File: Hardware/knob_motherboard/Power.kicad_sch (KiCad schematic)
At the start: 16 parts, among them J1 USB_C_Receptacle_USB2.0, U4 CH224K, U6 MT2492

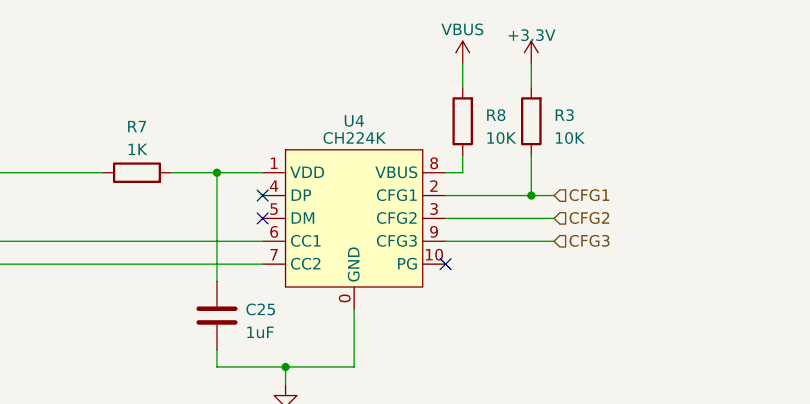
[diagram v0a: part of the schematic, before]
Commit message: drv8311 spi bugfix & ch224k CFG1 bugfix
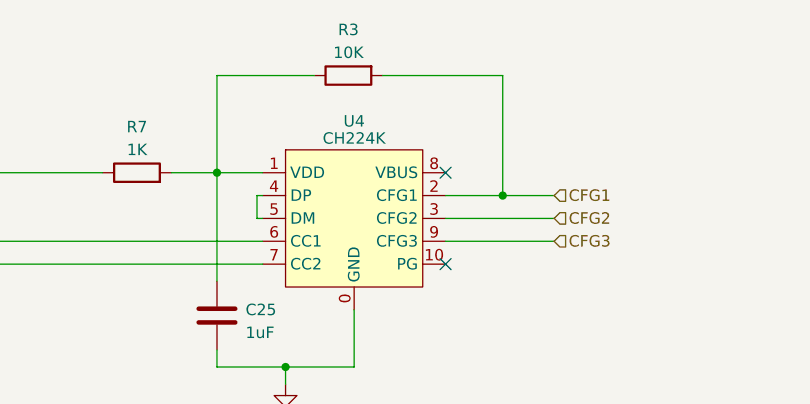
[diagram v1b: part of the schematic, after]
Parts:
- removed R8: 10K, Resistor_SMD:R_0402_1005Metric, symbol Device:R
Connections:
- net +3.3V is gone; now on net CFG1: R3.2
- net CFG1: no longer R3.1
- net at C25.1, R7.2, U4.1 (VDD): now also R3.1
- net at U4.4 (DP): now also U4.5 (DM)
- no-connect marks 5 -> 4
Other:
- moved on the sheet: R3
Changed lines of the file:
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@@
     (company "wirano")
   )
+  (junction (at 119.38 86.36) (diameter 0) (color 0 0 0 0)
+  )
   (junction (at 87.63 83.82) (diameter 0) (color 0 0 0 0)
-  )
-  (junction (at 122.555 86.36) (diameter 0) (color 0 0 0 0)
   )
   (junction (at 253.365 95.25) (diameter 0) (color 0 0 0 0)
@@
   (no_connect (at 57.15 116.84))
   (no_connect (at 113.03 93.98))
-  (no_connect (at 92.71 86.36))
-  (no_connect (at 92.71 88.9))
+  (no_connect (at 113.03 83.82))
   (wire (pts (xy 102.87 99.06) (xy 102.87 105.41))
     (stroke (width 0) (type default))
@@
     (stroke (width 0) (type default))
   )
-  (wire (pts (xy 114.935 81.915) (xy 114.935 83.82))
-    (stroke (width 0) (type default))
-  )
   (wire (pts (xy 34.29 124.46) (xy 34.29 125.73))
     (stroke (width 0) (type default))
@@
     (stroke (width 0) (type default))
   )
-  (wire (pts (xy 122.555 71.755) (xy 122.555 74.295))
-    (stroke (width 0) (type default))
-  )
   (wire (pts (xy 125.095 88.9) (xy 113.03 88.9))
     (stroke (width 0) (type default))
@@
     (stroke (width 0) (type default))
   )
-  (wire (pts (xy 113.03 83.82) (xy 114.935 83.82))
-    (stroke (width 0) (type default))
-  )
   (wire (pts (xy 266.7 95.25) (xy 266.7 92.71))
     (stroke (width 0) (type default))
@@
     (stroke (width 0) (type default))
   )
-  (wire (pts (xy 125.095 86.36) (xy 122.555 86.36))
-    (stroke (width 0) (type default))
-  )
   (wire (pts (xy 266.7 95.25) (xy 253.365 95.25))
     (stroke (width 0) (type default))
@@
     (stroke (width 0) (type default))
   )
-  (wire (pts (xy 114.935 71.755) (xy 114.935 74.295))
+  (wire (pts (xy 119.38 86.36) (xy 125.095 86.36))
     (stroke (width 0) (type default))
   )
@@
     (stroke (width 0) (type default))
   )
+  (wire (pts (xy 106.045 73.025) (xy 119.38 73.025))
+    (stroke (width 0) (type default))
+  )
   (wire (pts (xy 241.935 114.935) (xy 241.935 109.855))
     (stroke (width 0) (type default))
@@
     (stroke (width 0) (type default))
   )
+  (wire (pts (xy 92.075 86.36) (xy 92.075 88.9))
+    (stroke (width 0) (type default))
+  )
   (wire (pts (xy 222.885 95.25) (xy 233.045 95.25))
     (stroke (width 0) (type default))
@@
     (stroke (width 0) (type default))
   )
+  (wire (pts (xy 92.075 88.9) (xy 92.71 88.9))
+    (stroke (width 0) (type default))
+  )
+  (wire (pts (xy 119.38 73.025) (xy 119.38 86.36))
+    (stroke (width 0) (type default))
+  )
   (wire (pts (xy 253.365 102.235) (xy 253.365 95.25))
     (stroke (width 0) (type default))
@@
     (stroke (width 0) (type default))
   )
+  (wire (pts (xy 87.63 73.025) (xy 98.425 73.025))
+    (stroke (width 0) (type default))
+  )
   (wire (pts (xy 210.185 83.82) (xy 210.185 95.25))
     (stroke (width 0) (type default))
@@
     (stroke (width 0) (type default))
   )
-  (wire (pts (xy 113.03 86.36) (xy 122.555 86.36))
+  (wire (pts (xy 92.075 86.36) (xy 92.71 86.36))
+    (stroke (width 0) (type default))
+  )
+  (wire (pts (xy 113.03 86.36) (xy 119.38 86.36))
     (stroke (width 0) (type default))
   )
@@
     (stroke (width 0) (type default))
   )
+  (wire (pts (xy 87.63 73.025) (xy 87.63 83.82))
+    (stroke (width 0) (type default))
+  )
   (wire (pts (xy 95.25 105.41) (xy 95.25 107.315))
     (stroke (width 0) (type default))
@@
   )
   (wire (pts (xy 233.045 95.25) (xy 241.935 95.25))
-    (stroke (width 0) (type default))
-  )
-  (wire (pts (xy 122.555 81.915) (xy 122.555 86.36))
     (stroke (width 0) (type default))
   )
@@
     (effects (font (size 1.27 1.27)) (justify left))
   )
-  (symbol (lib_id "Device:R") (at 122.555 78.105 180) (unit 1)
-    (in_bom yes) (on_board yes) (dnp no) (fields_autoplaced)
-    (property "Reference" "R3" (at 125.095 77.47 0)
-      (effects (font (size 1.27 1.27)) (justify right))
-    )
-    (property "Value" "10K" (at 125.095 80.01 0)
-      (effects (font (size 1.27 1.27)) (justify right))
-    )
-    (property "Footprint" "Resistor_SMD:R_0402_1005Metric" (at 124.333 78.105 90)
-      (effects (font (size 1.27 1.27)) hide)
-    )
-    (property "Datasheet" "~" (at 122.555 78.105 0)
+  (symbol (lib_id "Device:R") (at 102.235 73.025 90) (mirror x) (unit 1)
+    (in_bom yes) (on_board yes) (dnp no)
+    (property "Reference" "R3" (at 102.235 67.945 90)
+      (effects (font (size 1.27 1.27)))
+    )
+    (property "Value" "10K" (at 102.235 70.485 90)
+      (effects (font (size 1.27 1.27)))
+    )
+    (property "Footprint" "Resistor_SMD:R_0402_1005Metric" (at 102.235 71.247 90)
+      (effects (font (size 1.27 1.27)) hide)
+    )
+    (property "Datasheet" "~" (at 102.235 73.025 0)
       (effects (font (size 1.27 1.27)) hide)
     )
@@
         (path "/85545740-8130-40e2-88f5-be9badfe8953/b008575e-1207-4067-b933-f7a58e4348ce"
           (reference "R10") (unit 1)
-        )
-      )
-    )
-  )
-  (symbol (lib_id "power:VBUS") (at 114.935 71.755 0) (unit 1)
-    (in_bom yes) (on_board yes) (dnp no) (fields_autoplaced)
-    (property "Reference" "#PWR032" (at 114.935 75.565 0)
-      (effects (font (size 1.27 1.27)) hide)
-    )
-    (property "Value" "VBUS" (at 114.935 67.945 0)
-      (effects (font (size 1.27 1.27)))
-    )
-    (property "Footprint" "" (at 114.935 71.755 0)
-      (effects (font (size 1.27 1.27)) hide)
-    )
-    (property "Datasheet" "" (at 114.935 71.755 0)
-      (effects (font (size 1.27 1.27)) hide)
-    )
-    (pin "1")
-    (instances
-      (project "haptic-knob"
-        (path "/85545740-8130-40e2-88f5-be9badfe8953/b008575e-1207-4067-b933-f7a58e4348ce"
-          (reference "#PWR032") (unit 1)
         )
       )
@@
     )
   )
-  (symbol (lib_id "power:+3.3V") (at 122.555 71.755 0) (unit 1)
-    (in_bom yes) (on_board yes) (dnp no) (fields_autoplaced)
-    (property "Reference" "#PWR011" (at 122.555 75.565 0)
-      (effects (font (size 1.27 1.27)) hide)
-    )
-    (property "Value" "+3.3V" (at 122.555 68.58 0)
-      (effects (font (size 1.27 1.27)))
-    )
-    (property "Footprint" "" (at 122.555 71.755 0)
-      (effects (font (size 1.27 1.27)) hide)
-    )
-    (property "Datasheet" "" (at 122.555 71.755 0)
-      (effects (font (size 1.27 1.27)) hide)
-    )
-    (pin "1")
-    (instances
-      (project "haptic-knob"
-        (path "/85545740-8130-40e2-88f5-be9badfe8953/b008575e-1207-4067-b933-f7a58e4348ce"
-          (reference "#PWR011") (unit 1)
-        )
-      )
-    )
-  )
   (symbol (lib_id "power:GND") (at 241.935 114.935 0) (unit 1)
     (in_bom yes) (on_board yes) (dnp no) (fields_autoplaced)
@@
         )
       )
-    )
-  )
-  (symbol (lib_id "Device:R") (at 114.935 78.105 180) (unit 1)
-    (in_bom yes) (on_board yes) (dnp no) (fields_autoplaced)
-    (property "Reference" "R8" (at 117.475 77.47 0)
-      (effects (font (size 1.27 1.27)) (justify right))
-    )
-    (property "Value" "10K" (at 117.475 80.01 0)
-      (effects (font (size 1.27 1.27)) (justify right))
-    )
-    (property "Footprint" "Resistor_SMD:R_0402_1005Metric" (at 116.713 78.105 90)
-      (effects (font (size 1.27 1.27)) hide)
-    )
-    (property "Datasheet" "~" (at 114.935 78.105 0)
-      (effects (font (size 1.27 1.27)) hide)
-    )
-    (pin "1")
-    (pin "2")
-    (instances
-      (project "haptic-knob"
-        (path "/85545740-8130-40e2-88f5-be9badfe8953/b008575e-1207-4067-b933-f7a58e4348ce"
-          (reference "R8") (unit 1)
-        )
-      )

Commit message: CH224K & ST77903 symbol fix
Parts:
- U4: footprint library:ESSOP-10_3.9x4.9mm_P1.00mm_EP2.3x3.2mm -> Library:ESSOP-10_3.9x4.9mm_P1.00mm_EP2.3x3.2mm
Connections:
- net CFG1: now also U4.9 (CFG1); no longer U4.2 (CFG1)
- net CFG2: now also U4.2 (CFG2); no longer U4.3 (CFG2)
- net CFG3: now also U4.3 (CFG3); no longer U4.9 (CFG3)
- net at U4.6 (CC2): now also J1.B5 (CC2); no longer J1.A5 (CC1)
- net at U4.7 (CC1): now also J1.A5 (CC1); no longer J1.B5 (CC2)
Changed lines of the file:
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@@
-(kicad_sch (version 20230221) (generator eeschema)
+(kicad_sch (version 20230409) (generator eeschema)
   (paper "A4")
   (title_block
@@
   )
   (text_box "R10=R9/(V_{OUT}/V_{FB}-1)"
-    (at 212.725 112.395 0) (size 26.67 3.81)
+    (exclude_from_sim no) (at 212.725 112.395 0) (size 26.67 3.81)
     (stroke (width 0) (type default))
     (fill (type color) (color 255 255 194 1))
@@
   )
   (text_box "Under light load conditions below 100mA, larger inductance is recommended for improved efficiency."
-    (at 220.345 83.82 0) (size 30.48 10.16)
+    (exclude_from_sim no) (at 220.345 83.82 0) (size 30.48 10.16)
     (stroke (width 0) (type default))
     (fill (type color) (color 255 255 194 1))
@@
       (effects (font (size 1.27 1.27)))
     )
-    (property "Footprint" "library:ESSOP-10_3.9x4.9mm_P1.00mm_EP2.3x3.2mm" (at 104.14 107.95 0)
-      (effects (font (size 1.27 1.27)) hide)
-    )
-    (property "Datasheet" "https://www.wch.cn/downloads/file/301.html?time=2023-02-06%2019:34:56&code=XDyYZVEGtumLwxyJajinU25wFKSw1uRtrayaPDIv" (at 104.14 110.49 0)
-      (effects (font (size 1.27 1.27)) hide)
-    )
+    (property "Footprint" "Library:ESSOP-10_3.9x4.9mm_P1.00mm_EP2.3x3.2mm" (at 104.14 107.95 0)
+      (effects (font (size 1.27 1.27)) hide)
+    )
+    (property "Datasheet" "https://www.wch.cn/downloads/CH224DS1_PDF.html" (at 104.14 110.49 0)
+      (effects (font (size 1.27 1.27)) hide)
+    )
